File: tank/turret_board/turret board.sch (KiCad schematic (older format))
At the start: 24 parts, among them J1 Conn_01x06, J2 Conn_01x06, J3 Conn_01x02_Male, Q1 2N3904, Q2 2N3904, U1 KA378R33, U2 pixart_ir, Y1 Crystal_4pin

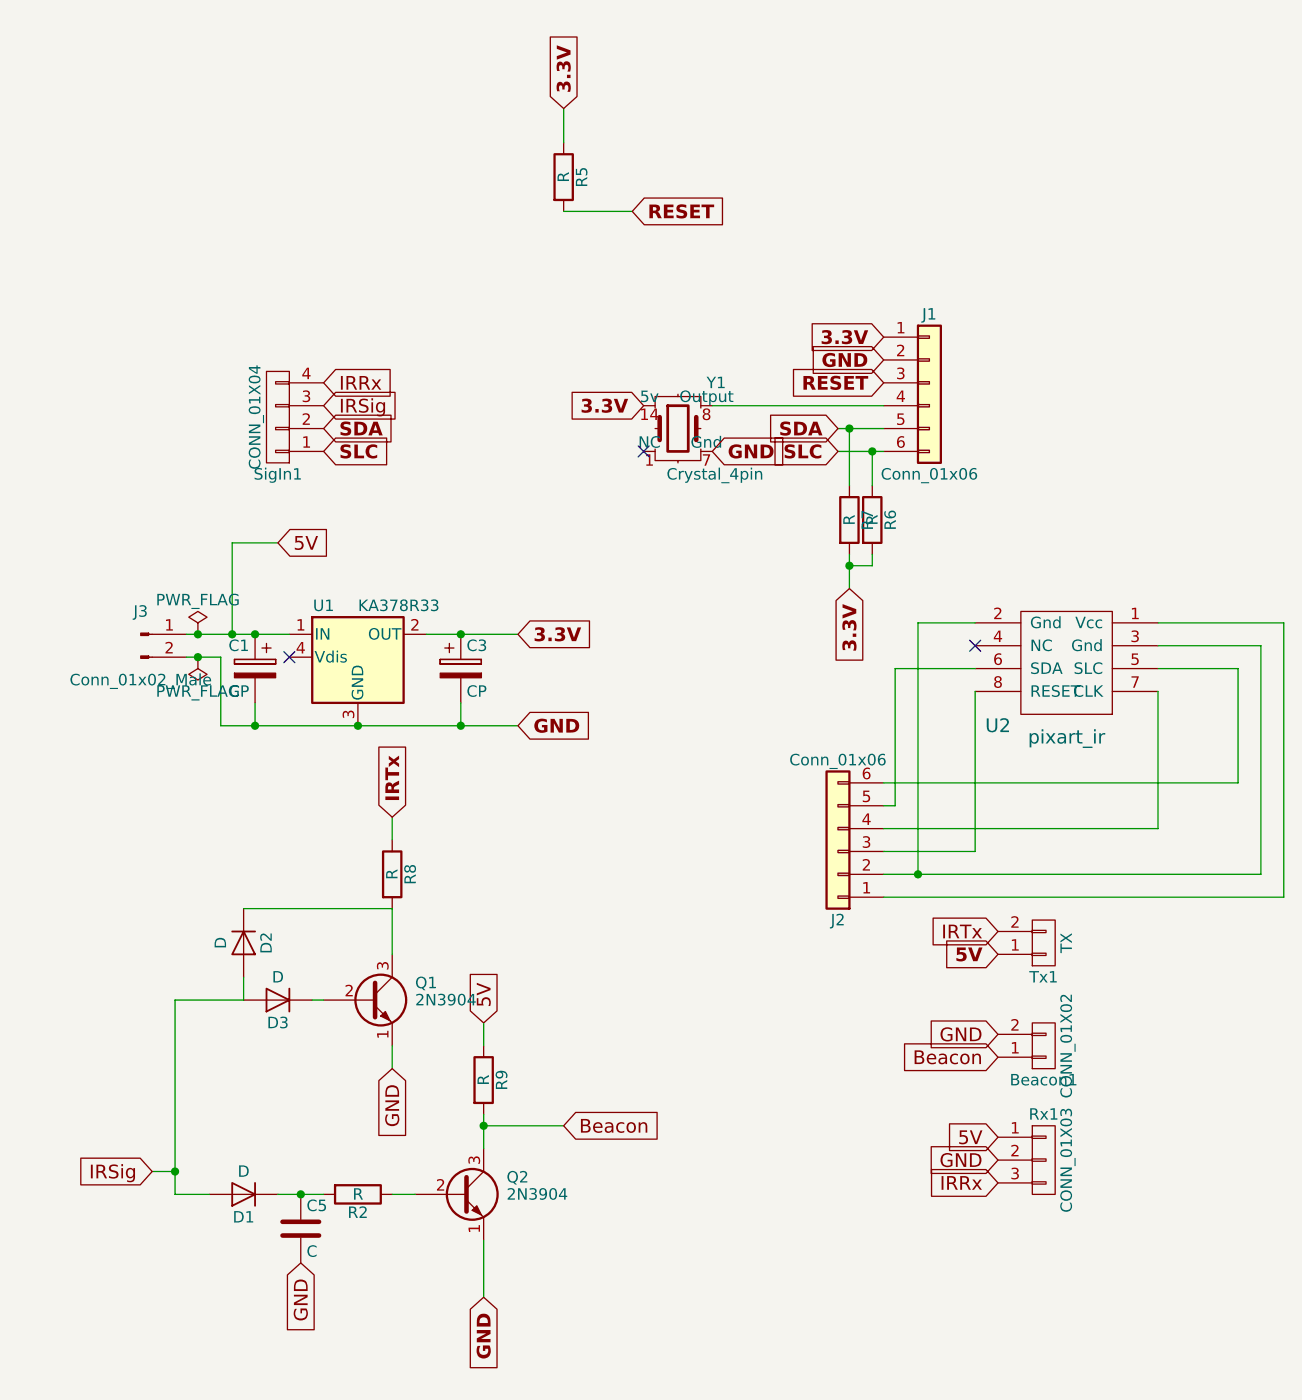
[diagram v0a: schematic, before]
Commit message: Turret board version 0.5: - camera is integrated onto board
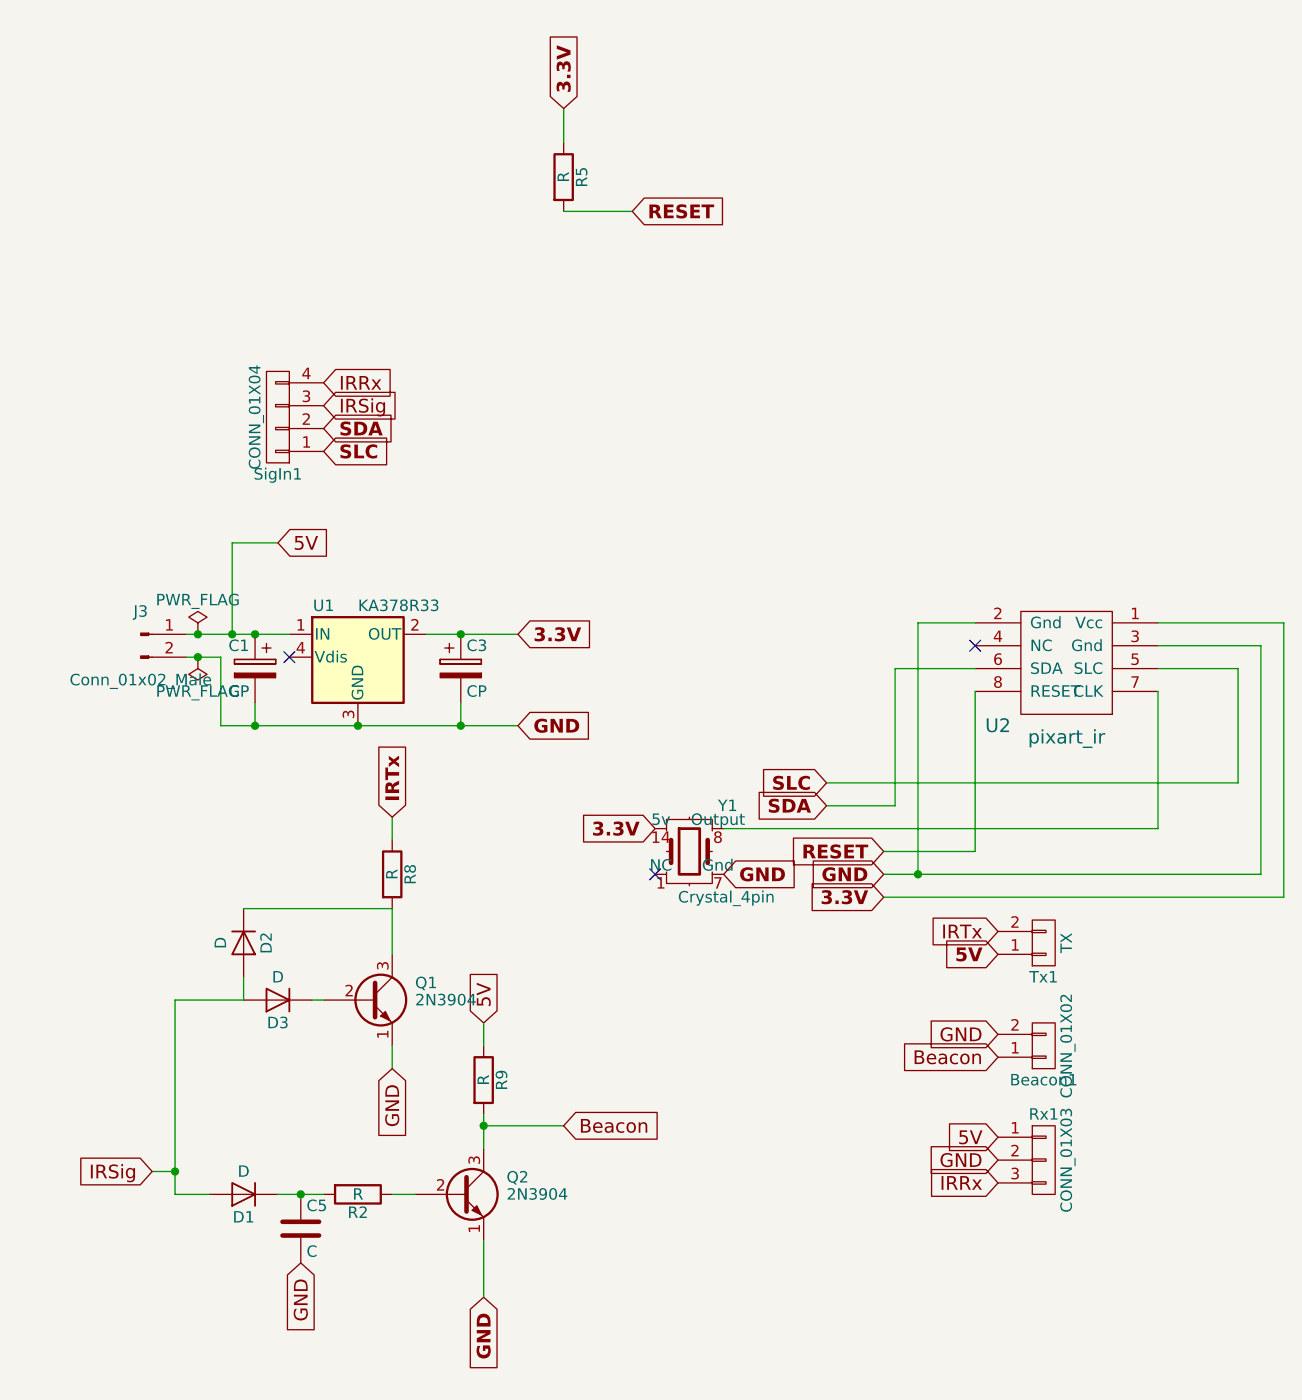
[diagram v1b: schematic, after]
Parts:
- removed J1, J2: Conn_01x06, Pin_Headers:Pin_Header_Straight_2x03_Pitch2.54mm, symbol miar_labs:Conn_01x06
- removed R6, R7: R, Resistors_THT:R_Axial_DIN0207_L6.3mm_D2.5mm_P7.62mm_Horizontal, symbol miar_labs:R
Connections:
- net 3.3V: now also U2.1 (Vcc)
- net GND: now also U2.2 (Gnd), U2.3 (Gnd)
- net RESET: now also U2.8 (RESET)
- net SDA: now also U2.6 (SDA)
- net SLC: now also U2.5 (SLC)
- net at U2.7 (CLK): now also Y1.8 (Output)
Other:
- moved on the sheet: Y1
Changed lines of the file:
@@
-$EndComp
-$Comp
-L miar_labs:R R7
-U 1 1 59D66D74
-P 4150 2550
-F 0 "R7" V 4230 2550 50  0000 C CNN
-F 1 "R" V 4150 2550 50  0000 C CNN
-F 2 "Resistors_THT:R_Axial_DIN0207_L6.3mm_D2.5mm_P7.62mm_Horizontal" V 4080 2550 50  0001 C CNN
-F 3 "" H 4150 2550 50  0000 C CNN
-	1    4150 2550
-	1    0    0    -1
-$EndComp
-$Comp
-L miar_labs:R R6
-U 1 1 59D66E03
-P 4250 2550
-F 0 "R6" V 4330 2550 50  0000 C CNN
-F 1 "R" V 4250 2550 50  0000 C CNN
-F 2 "Resistors_THT:R_Axial_DIN0207_L6.3mm_D2.5mm_P7.62mm_Horizontal" V 4180 2550 50  0001 C CNN
-F 3 "" H 4250 2550 50  0000 C CNN
-	1    4250 2550
-	1    0    0    -1
 $EndComp
 $Comp
 L custom:Crystal_4pin Y1
 U 1 1 59D70B97
-P 3400 2150
-F 0 "Y1" H 3525 2350 50  0000 L CNN
-F 1 "Crystal_4pin" H 3350 1950 50  0000 L CNN
-F 2 "Tank:ECS-100AX" H 3400 2150 50  0001 C CNN
-F 3 "" H 3400 2150 50  0001 C CNN
-	1    3400 2150
-	1    0    0    -1
-$EndComp
-NoConn ~ 3250 2250
+P 3450 4000
+F 0 "Y1" H 3575 4200 50  0000 L CNN
+F 1 "Crystal_4pin" H 3400 3800 50  0000 L CNN
+F 2 "Tank:ECS-100AX" H 3450 4000 50  0001 C CNN
+F 3 "" H 3450 4000 50  0001 C CNN
+	1    3450 4000
+	1    0    0    -1
+$EndComp
+NoConn ~ 3300 4100
 $Comp
 L power:PWR_FLAG #FLG01
@@
 Text GLabel 2550 5950 3    60   Input ~ 12
 GND
-$Comp
-L miar_labs:Conn_01x06 J1
-U 1 1 59ED8021
-P 4500 1950
-F 0 "J1" H 4500 2250 50  0000 C CNN
-F 1 "Conn_01x06" H 4500 1550 50  0000 C CNN
-F 2 "Pin_Headers:Pin_Header_Straight_2x03_Pitch2.54mm" H 4500 1950 50  0001 C CNN
-F 3 "" H 4500 1950 50  0001 C CNN
-	1    4500 1950
-	1    0    0    -1
-$EndComp
-Text GLabel 4300 1750 0    60   Input ~ 12
-3.3V
-Text GLabel 4300 1850 0    60   Input ~ 12
-GND
-Text GLabel 4300 1950 0    60   Input ~ 12
-RESET
-Text GLabel 4100 2150 0    60   Input ~ 12
-SDA
-Text GLabel 4100 2250 0    60   Input ~ 12
-SLC
-Text GLabel 3550 2250 2    60   Input ~ 12
-GND
-Text GLabel 3250 2050 0    60   Input ~ 12
+Text GLabel 3600 4100 2    60   Input ~ 12
+GND
+Text GLabel 3300 3900 0    60   Input ~ 12
 3.3V
 Text GLabel 3200 1200 2    60   Input ~ 12
 RESET
 Text GLabel 2700 3050 2    60   Input ~ 12
-3.3V
-Text GLabel 4150 2850 3    60   Input ~ 12
 3.3V
 Text GLabel 2900 750  1    60   Input ~ 12
@@
 Text GLabel 2700 3450 2    60   Input ~ 12
 GND
-$Comp
-L miar_labs:Conn_01x06 J2
-U 1 1 59EDA984
-P 4100 4000
-F 0 "J2" H 4100 4300 50  0000 C CNN
-F 1 "Conn_01x06" H 4100 3600 50  0000 C CNN
-F 2 "Pin_Headers:Pin_Header_Straight_2x03_Pitch2.54mm" H 4100 4000 50  0001 C CNN
-F 3 "" H 4100 4000 50  0001 C CNN
-	1    4100 4000
-	-1   0    0    1
-$EndComp
 NoConn ~ 4700 3100
 $Comp
@@
 	2150 3950 2150 3850
 Wire Wire Line
-	3550 2050 4300 2050
-Wire Wire Line
-	4100 2150 4150 2150
-Wire Wire Line
-	4100 2250 4250 2250
-Wire Wire Line
-	4150 2150 4150 2400
-Connection ~ 4150 2150
-Wire Wire Line
-	4250 2250 4250 2400
-Connection ~ 4250 2250
-Wire Wire Line
-	4150 2700 4150 2750
-Wire Wire Line
-	4150 2750 4250 2750
-Wire Wire Line
-	4250 2750 4250 2700
-Connection ~ 4150 2750
-Wire Wire Line
 	5500 3000 6050 3000
 Wire Wire Line
@@
 	4350 3200 4350 3800
 Wire Wire Line
-	4350 3800 4300 3800
-Wire Wire Line
 	5500 3200 5850 3200
 Wire Wire Line
 	5850 3200 5850 3700
 Wire Wire Line
-	5850 3700 4300 3700
-Wire Wire Line
 	4700 3300 4700 4000
 Wire Wire Line
@@
 Wire Wire Line
 	5500 3300 5500 3900
-Wire Wire Line
-	5500 3900 4300 3900
 Wire Wire Line
 	1250 3050 1300 3050
@@
 	2550 5200 2550 5300
 Wire Wire Line
-	4150 2150 4300 2150
-Wire Wire Line
-	4250 2250 4300 2250
-Wire Wire Line
-	4150 2750 4150 2850
-Wire Wire Line
 	4450 4100 5950 4100
 Wire Wire Line
@@
 Wire Wire Line
 	1450 3050 1550 3050
+Text GLabel 4050 3700 0    60   Input ~ 12
+SLC
+Text GLabel 4050 3800 0    60   Input ~ 12
+SDA
+Text GLabel 4300 4200 0    60   Input ~ 12
+3.3V
+Text GLabel 4300 4100 0    60   Input ~ 12
+GND
+Text GLabel 4300 4000 0    60   Input ~ 12
+RESET
+Wire Wire Line
+	3600 3900 5500 3900
+Wire Wire Line
+	4050 3800 4350 3800
+Wire Wire Line
+	4050 3700 5850 3700
 $EndSCHEMATC

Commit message: turret board interim
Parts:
- removed C1: CP, Capacitors_THT:CP_Radial_D5.0mm_P2.00mm, symbol miar_labs:CP
- removed Rx1: CONN_01X03, JST:JST_EH_B03B-EH-A_03x2.50mm_Straight, symbol miar_labs:CONN_01X03
- added C1: C_Small, Capacitors_THT:C_Disc_D3.0mm_W1.6mm_P2.50mm, symbol Device:C_Small
- added P1: CONN_01X02, JST:JST_EH_B02B-EH-A_02x2.50mm_Straight, symbol miar_labs:CONN_01X02
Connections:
- net 5V: now also P1.2 (P2); no longer J3.1 (Pin_1), U1.1 (IN)
- net GND: now also C1.2, P1.1 (P1)
- new net: C1.1, J3.1 (Pin_1), U1.1 (IN)
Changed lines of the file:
@@
 $EndDescr
-$Comp
-L miar_labs:CP C1
-U 1 1 59C1A5FB
-P 1550 3200
-F 0 "C1" H 1575 3300 50  0000 L CNN
-F 1 "CP" H 1575 3100 50  0000 L CNN
-F 2 "Capacitors_THT:CP_Radial_D5.0mm_P2.00mm" H 1588 3050 50  0001 C CNN
-F 3 "" H 1550 3200 50  0001 C CNN
-	1    1550 3200
-	-1   0    0    -1
-$EndComp
 $Comp
 L custom:pixart_ir U2
@@
 $EndComp
 $Comp
-L miar_labs:CONN_01X02 Beacon1
-U 1 1 59D648C7
-P 5000 4850
-F 0 "Beacon1" H 5000 5000 50  0000 C CNN
-F 1 "CONN_01X02" V 5100 4850 50  0000 C CNN
-F 2 "JST:JST_EH_B02B-EH-A_02x2.50mm_Straight" H 5000 4850 50  0001 C CNN
-F 3 "" H 5000 4850 50  0000 C CNN
-	1    5000 4850
-	1    0    0    1
-$EndComp
-$Comp
-L miar_labs:CONN_01X03 Rx1
-U 1 1 59D6497D
-P 5000 5350
-F 0 "Rx1" H 5000 5550 50  0000 C CNN
-F 1 "CONN_01X03" V 5100 5350 50  0000 C CNN
-F 2 "JST:JST_EH_B03B-EH-A_03x2.50mm_Straight" H 5000 5350 50  0001 C CNN
-F 3 "" H 5000 5350 50  0000 C CNN
-	1    5000 5350
-	1    0    0    -1
-$EndComp
-$Comp
 L miar_labs:CONN_01X02 Tx1
 U 1 1 59D64A36
@@
 	1    0    0    -1
 $EndComp
-Text GLabel 4800 4800 0    60   Input ~ 0
-GND
 Text GLabel 4800 4350 0    60   Input ~ 0
 IRTx
-Text GLabel 4800 5250 0    60   Input ~ 0
-5V
-Text GLabel 4800 5350 0    60   Input ~ 0
-GND
 Text GLabel 1100 5400 0    60   Input ~ 0
 IRSig
@@
 5V
 Text GLabel 2900 5200 2    60   Input ~ 0
-Beacon
-Text GLabel 4800 4900 0    60   Input ~ 0
 Beacon
 $Comp
@@
 Connection ~ 2450 3050
 Connection ~ 2000 3450
-Connection ~ 1550 3050
 Wire Wire Line
 	1200 4650 1200 5400
-Text GLabel 4800 5450 0    60   Input ~ 0
-IRRx
 Text GLabel 1850 1950 2    60   Input ~ 0
 IRRx
@@
 Connection ~ 1300 3150
 Wire Wire Line
-	1450 3050 1450 2650
-Wire Wire Line
-	1450 2650 1650 2650
-Connection ~ 1450 3050
-Text GLabel 1650 2650 2    60   Input ~ 0
-5V
-Wire Wire Line
 	1200 5400 1200 5500
 Wire Wire Line
@@
 	2000 3450 2450 3450
 Wire Wire Line
-	1550 3050 1700 3050
-Wire Wire Line
-	1300 3050 1450 3050
-Wire Wire Line
 	1300 3150 1400 3150
-Wire Wire Line
-	1450 3050 1550 3050
 Text GLabel 4050 3700 0    60   Input ~ 12
 SLC
@@
 Wire Wire Line
 	4050 3700 5850 3700
+Text GLabel 4800 4900 0    60   Input ~ 0
+Beacon
+Text GLabel 4800 4800 0    60   Input ~ 0
+GND
+$Comp
+L miar_labs:CONN_01X02 Beacon1
+U 1 1 59D648C7
+P 5000 4850
+F 0 "Beacon1" H 5000 5000 50  0000 C CNN
+F 1 "CONN_01X02" V 5100 4850 50  0000 C CNN
+F 2 "JST:JST_EH_B02B-EH-A_02x2.50mm_Straight" H 5000 4850 50  0001 C CNN
+F 3 "" H 5000 4850 50  0000 C CNN
+	1    5000 4850
+	1    0    0    1
+$EndComp
+$Comp
+L miar_labs:CONN_01X02 P1
+U 1 1 5EE440E3
+P 1650 1600
+F 0 "P1" H 1567 1325 50  0000 C CNN
+F 1 "CONN_01X02" H 1567 1416 50  0000 C CNN
+F 2 "JST:JST_EH_B02B-EH-A_02x2.50mm_Straight" H 1650 1600 50  0001 C CNN
+F 3 "" H 1650 1600 50  0000 C CNN
+	1    1650 1600
+	-1   0    0    1
+$EndComp
+Text GLabel 1850 1550 2    50   Input ~ 0
+5V
+Text GLabel 1850 1650 2    50   Input ~ 0
+GND
+Text GLabel 1050 3050 0    50   Input ~ 0
+5V
+Text GLabel 1050 3150 0    50   Input ~ 0
+GND
+$Comp
+L Device:C_Small C1
+U 1 1 5EE472A7
+P 1550 3250
+F 0 "C1" H 1642 3296 50  0000 L CNN
+F 1 "C_Small" H 1642 3205 50  0000 L CNN
+F 2 "Capacitors_THT:C_Disc_D3.0mm_W1.6mm_P2.50mm" H 1550 3250 50  0001 C CNN
+F 3 "~" H 1550 3250 50  0001 C CNN
+	1    1550 3250
+	1    0    0    -1
+$EndComp
+Wire Wire Line
+	1550 3150 1550 3050
+Connection ~ 1550 3050
+Wire Wire Line
+	1550 3050 1700 3050
+Wire Wire Line
+	1300 3050 1550 3050
 $EndSCHEMATC

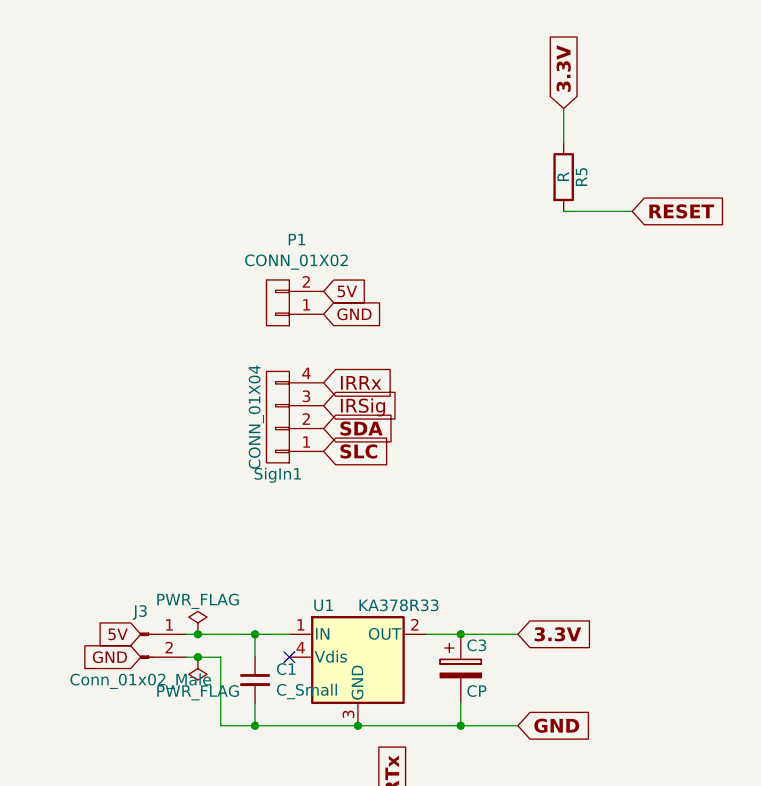
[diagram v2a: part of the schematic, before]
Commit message: Turret Board Version 0.6: - change camera orientation to better fit in turret - updated footprints
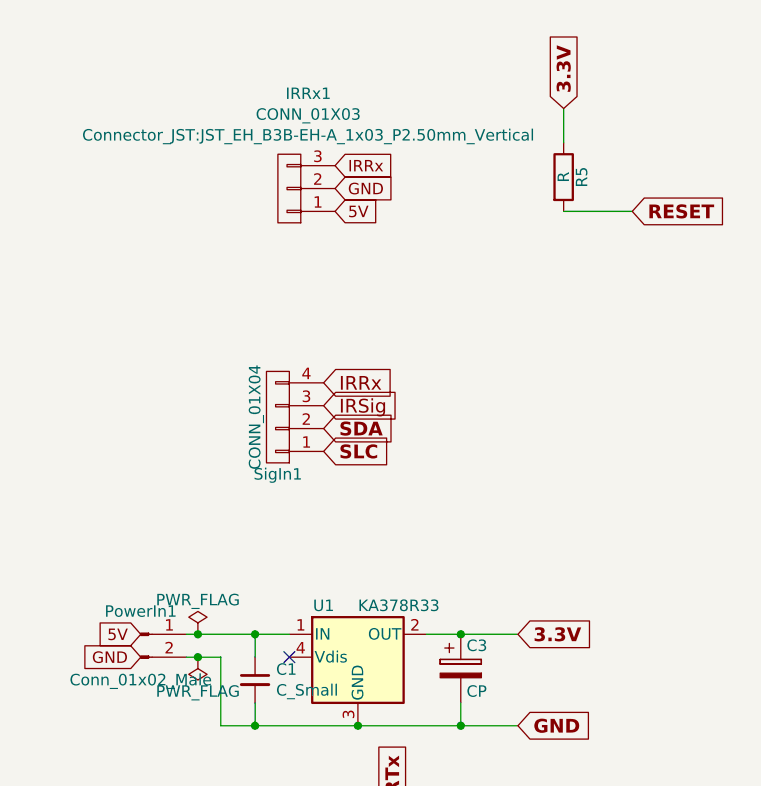
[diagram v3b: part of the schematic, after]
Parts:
- removed P1: CONN_01X02, JST:JST_EH_B02B-EH-A_02x2.50mm_Straight, symbol miar_labs:CONN_01X02
- added IRRx1: CONN_01X03, Connector_JST:JST_EH_B3B-EH-A_1x03_P2.50mm_Vertical, symbol miar_labs:CONN_01X03
- Beacon1, Tx1: footprint JST:JST_EH_B02B-EH-A_02x2.50mm_Straight -> Connector_JST:JST_EH_B2B-EH-A_1x02_P2.50mm_Vertical
- C1: footprint Capacitors_THT:C_Disc_D3.0mm_W1.6mm_P2.50mm -> Capacitor_THT:C_Disc_D4.7mm_W2.5mm_P5.00mm
- R8: footprint Resistors_THT:R_Axial_DIN0207_L6.3mm_D2.5mm_P7.62mm_Horizontal -> Resistor_THT:R_Axial_DIN0207_L6.3mm_D2.5mm_P7.62mm_Horizontal
- SigIn1: footprint JST:JST_EH_B04B-EH-A_04x2.50mm_Straight -> Connector_JST:JST_EH_B4B-EH-A_1x04_P2.50mm_Vertical
- renumbered J3 to PowerIn1
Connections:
- net 5V: now also IRRx1.1 (P1)
- net GND: now also IRRx1.2 (P2)
- net IRRx: now also IRRx1.3 (P3)
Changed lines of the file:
@@
 F 0 "SigIn1" H 1650 2350 50  0000 C CNN
 F 1 "CONN_01X04" V 1750 2100 50  0000 C CNN
-F 2 "JST:JST_EH_B04B-EH-A_04x2.50mm_Straight" H 1650 2100 50  0001 C CNN
+F 2 "Connector_JST:JST_EH_B4B-EH-A_1x04_P2.50mm_Vertical" H 1650 2100 50  0001 C CNN
 F 3 "" H 1650 2100 50  0000 C CNN
 	1    1650 2100
@@
 F 0 "Tx1" H 5000 4550 50  0000 C CNN
 F 1 "TX" V 5100 4400 50  0000 C CNN
-F 2 "JST:JST_EH_B02B-EH-A_02x2.50mm_Straight" H 5000 4400 50  0001 C CNN
+F 2 "Connector_JST:JST_EH_B2B-EH-A_1x02_P2.50mm_Vertical" H 5000 4400 50  0001 C CNN
 F 3 "" H 5000 4400 50  0000 C CNN
 	1    5000 4400
@@
 F 0 "R8" V 2230 4100 50  0000 C CNN
 F 1 "R" V 2150 4100 50  0000 C CNN
-F 2 "Resistors_THT:R_Axial_DIN0207_L6.3mm_D2.5mm_P7.62mm_Horizontal" V 2080 4100 50  0001 C CNN
+F 2 "Resistor_THT:R_Axial_DIN0207_L6.3mm_D2.5mm_P7.62mm_Horizontal" V 2080 4100 50  0001 C CNN
 F 3 "" H 2150 4100 50  0001 C CNN
 	1    2150 4100
@@
 NoConn ~ 1700 3150
 $Comp
-L miar_labs:Conn_01x02_Male J3
+L miar_labs:Conn_01x02_Male PowerIn1
 U 1 1 5A07DE3C
 P 1050 3050
-F 0 "J3" H 1050 3150 50  0000 C CNN
+F 0 "PowerIn1" H 1050 3150 50  0000 C CNN
 F 1 "Conn_01x02_Male" H 1050 2850 50  0000 C CNN
 F 2 "JST:JST_EH_B02B-EH-A_02x2.50mm_Straight" H 1050 3050 50  0001 C CNN
@@
 F 0 "Beacon1" H 5000 5000 50  0000 C CNN
 F 1 "CONN_01X02" V 5100 4850 50  0000 C CNN
-F 2 "JST:JST_EH_B02B-EH-A_02x2.50mm_Straight" H 5000 4850 50  0001 C CNN
+F 2 "Connector_JST:JST_EH_B2B-EH-A_1x02_P2.50mm_Vertical" H 5000 4850 50  0001 C CNN
 F 3 "" H 5000 4850 50  0000 C CNN
 	1    5000 4850
 	1    0    0    1
 $EndComp
-$Comp
-L miar_labs:CONN_01X02 P1
-U 1 1 5EE440E3
-P 1650 1600
-F 0 "P1" H 1567 1325 50  0000 C CNN
-F 1 "CONN_01X02" H 1567 1416 50  0000 C CNN
-F 2 "JST:JST_EH_B02B-EH-A_02x2.50mm_Straight" H 1650 1600 50  0001 C CNN
-F 3 "" H 1650 1600 50  0000 C CNN
-	1    1650 1600
-	-1   0    0    1
-$EndComp
-Text GLabel 1850 1550 2    50   Input ~ 0
-5V
-Text GLabel 1850 1650 2    50   Input ~ 0
-GND
 Text GLabel 1050 3050 0    50   Input ~ 0
 5V
@@
 F 0 "C1" H 1642 3296 50  0000 L CNN
 F 1 "C_Small" H 1642 3205 50  0000 L CNN
-F 2 "Capacitors_THT:C_Disc_D3.0mm_W1.6mm_P2.50mm" H 1550 3250 50  0001 C CNN
+F 2 "Capacitor_THT:C_Disc_D4.7mm_W2.5mm_P5.00mm" H 1550 3250 50  0001 C CNN
 F 3 "~" H 1550 3250 50  0001 C CNN
 	1    1550 3250
@@
 Wire Wire Line
 	1300 3050 1550 3050
+$Comp
+L miar_labs:CONN_01X03 IRRx1
+U 1 1 615322E3
+P 1700 1100
+F 0 "IRRx1" H 1617 685 50  0000 C CNN
+F 1 "CONN_01X03" H 1617 776 50  0000 C CNN
+F 2 "Connector_JST:JST_EH_B3B-EH-A_1x03_P2.50mm_Vertical" H 1617 867 50  0000 C CNN
+F 3 "" H 1700 1100 50  0000 C CNN
+	1    1700 1100
+	-1   0    0    1
+$EndComp
+Text GLabel 1900 1000 2    50   Input ~ 0
+IRRx
+Text GLabel 1900 1200 2    50   Input ~ 0
+5V
+Text GLabel 1900 1100 2    50   Input ~ 0
+GND
 $EndSCHEMATC
